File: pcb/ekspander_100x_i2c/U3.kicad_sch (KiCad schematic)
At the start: 51 parts, among them J10 DG127A-5.08-06P-14-00AH, J11 DG127A-5.08-06P-14-00AH, J8 DG127A-5.08-06P-14-00AH, J9 DG127A-5.08-06P-14-00AH, U19 LTV-847, U20 LTV-847, U21 ITS716G, U22 ITS716G, U23 ITS716G, U24 ITS716G, U25 LTV-847, U3 MCP23017_SP, U4 MCP23017_SP

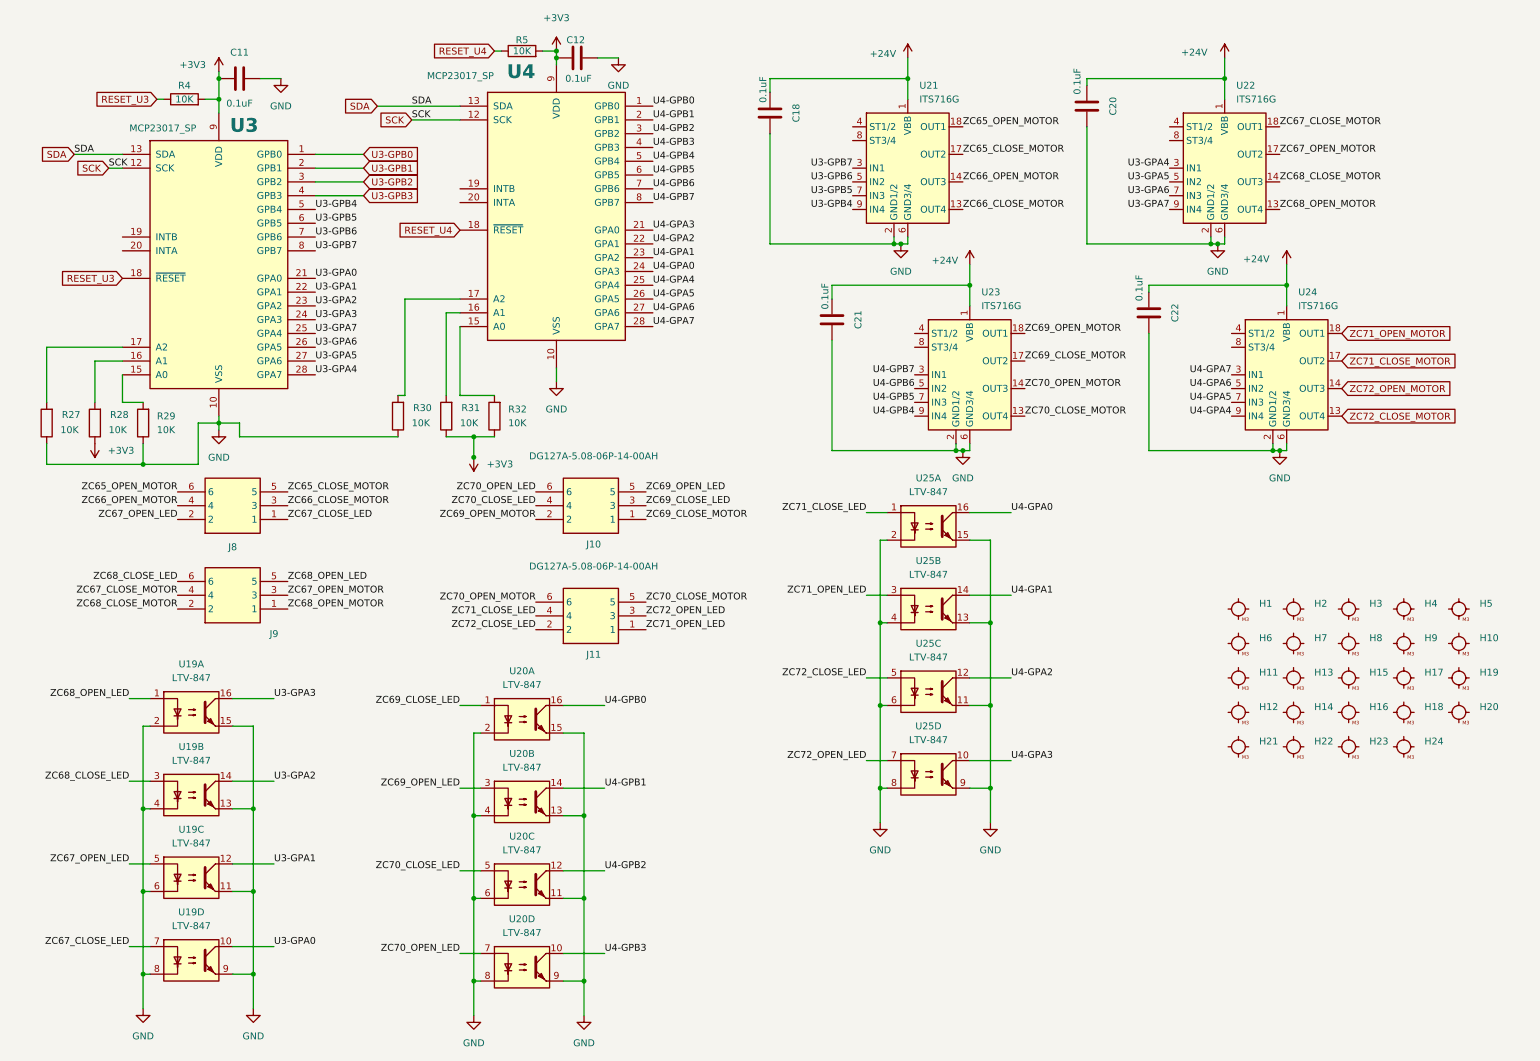
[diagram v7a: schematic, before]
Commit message: Ekspander 100x - diagnostic LEDs
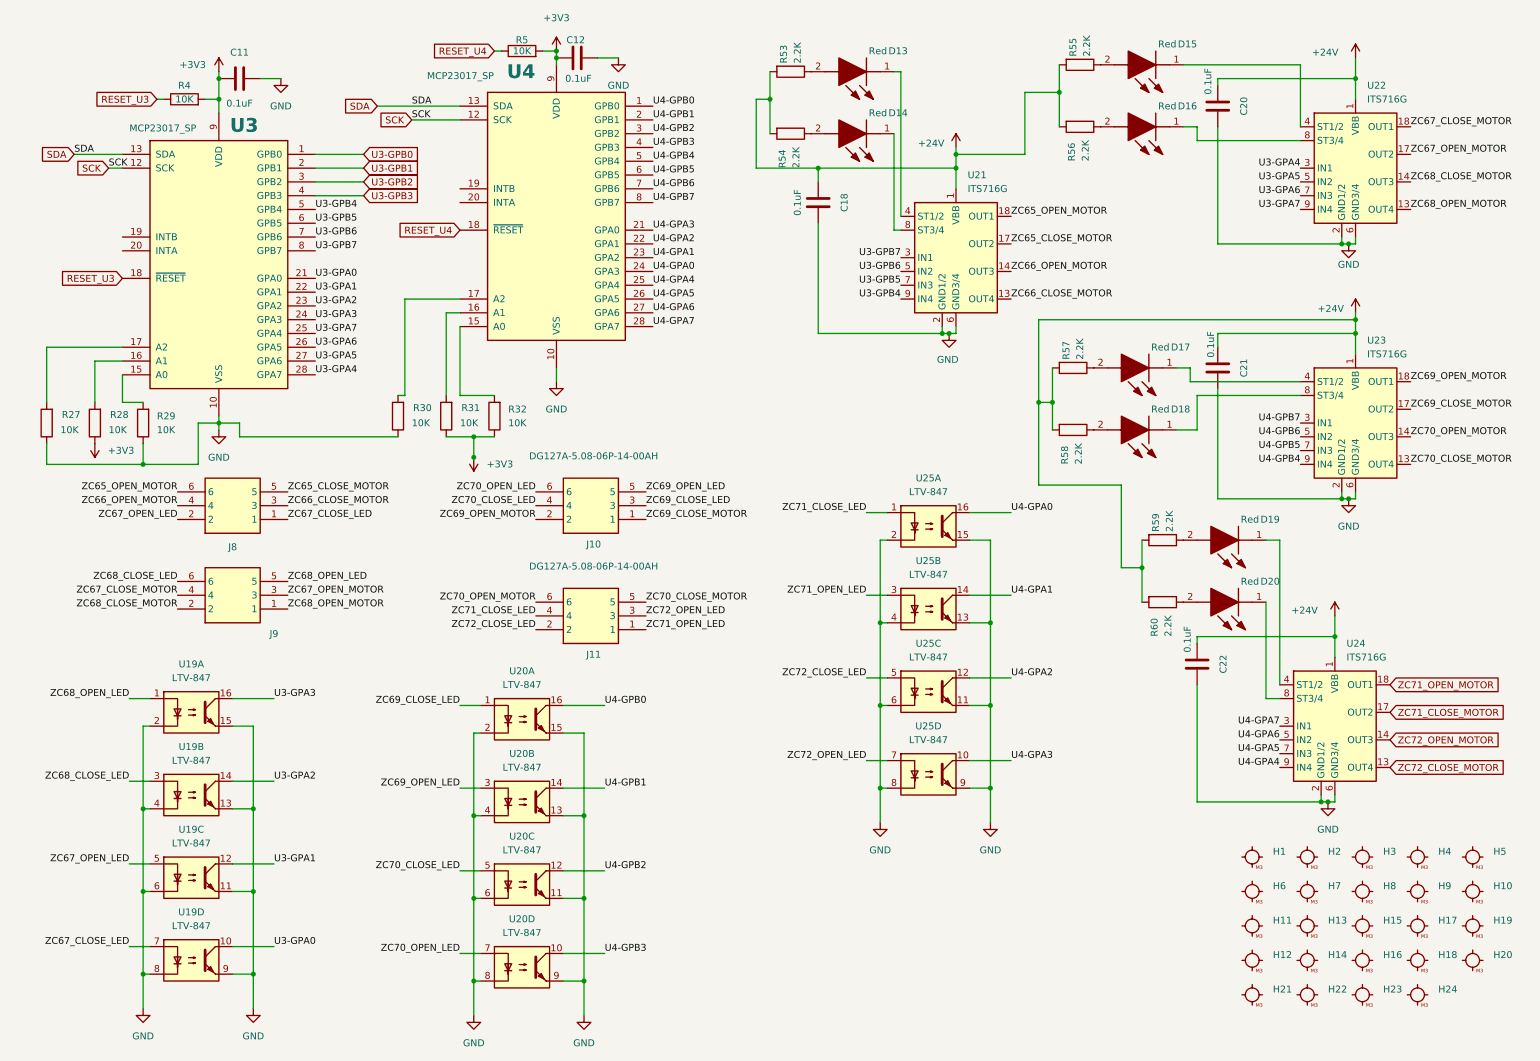
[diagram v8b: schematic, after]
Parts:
- added D13, D14, D15, D16, D17, D18, D19, D20: Red, 1_tme:LEDC2012X120N, symbol LTST-C170KRKT:LTST-C170KRKT
- added R53, R54, R55, R56, R57, R58, R59, R60: 2.2K, PCM_Resistor_SMD_AKL:R_0805_2012Metric_Pad1.20x1.40mm_HandSolder, symbol Device:R
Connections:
- net +24V: now also R53.2, R54.2, R55.2, R56.2, R57.2, R58.2, R59.2, R60.2
- net at U21.4 (ST1/2): now also D13.1 (K)
- net at U21.8 (ST3/4): now also D14.1 (K)
- net at U23.4 (ST1/2): now also D17.1 (K)
- net at U23.8 (ST3/4): now also D18.1 (K)
- net at U22.4 (ST1/2): now also D15.1 (K)
- net at U22.8 (ST3/4): now also D16.1 (K)
- net at U24.4 (ST1/2): now also D19.1 (K)
- net at U24.8 (ST3/4): now also D20.1 (K)
- new net: D15.2 (A), R55.1
- new net: D13.2 (A), R53.1
- new net: D19.2 (A), R59.1
- new net: D18.2 (A), R58.1
- new net: D17.2 (A), R57.1
- new net: D20.2 (A), R60.1
- new net: D14.2 (A), R54.1
- new net: D16.2 (A), R56.1
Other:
- moved on the sheet: C18, C20, C21, C22, H1, H10, H11, H12, H13, H14, H15, H16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
